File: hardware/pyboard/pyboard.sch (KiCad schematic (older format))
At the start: 71 parts, among them J1 Battery, J10 P9-P10, J2 Y1-Y8, J3 X9-X16, J4 P1-P8, J5 X17-X24, J6 USB_B_Micro, J7 Y9-Y16, J8 X1-X8, J9 Micro_SD_SCHA5B0200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

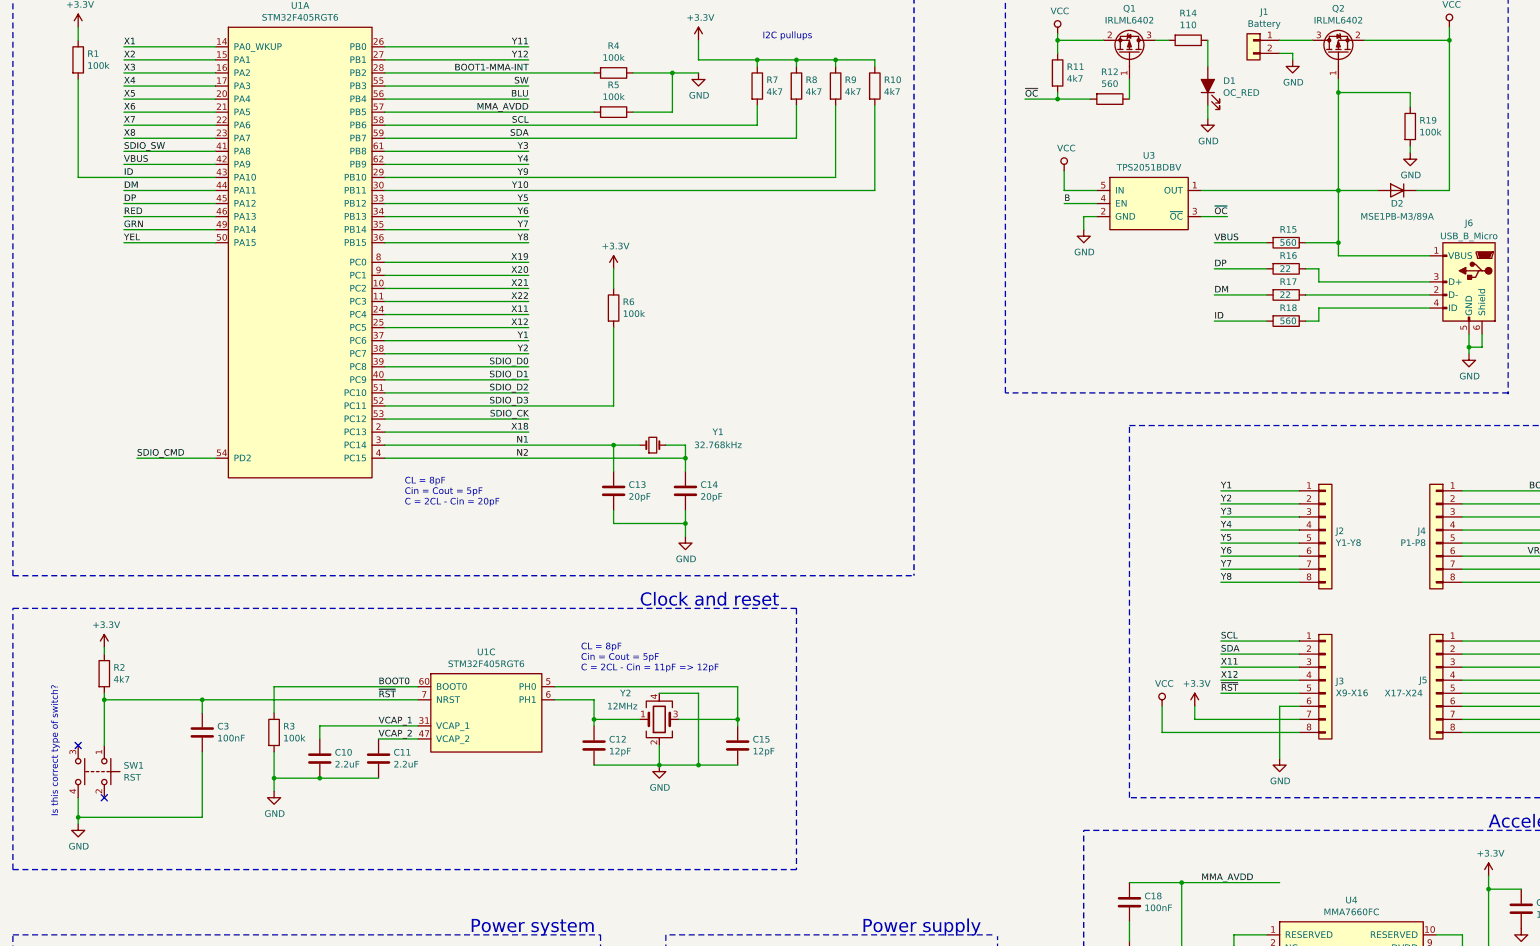
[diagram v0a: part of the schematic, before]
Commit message: Add pushbutton footprint
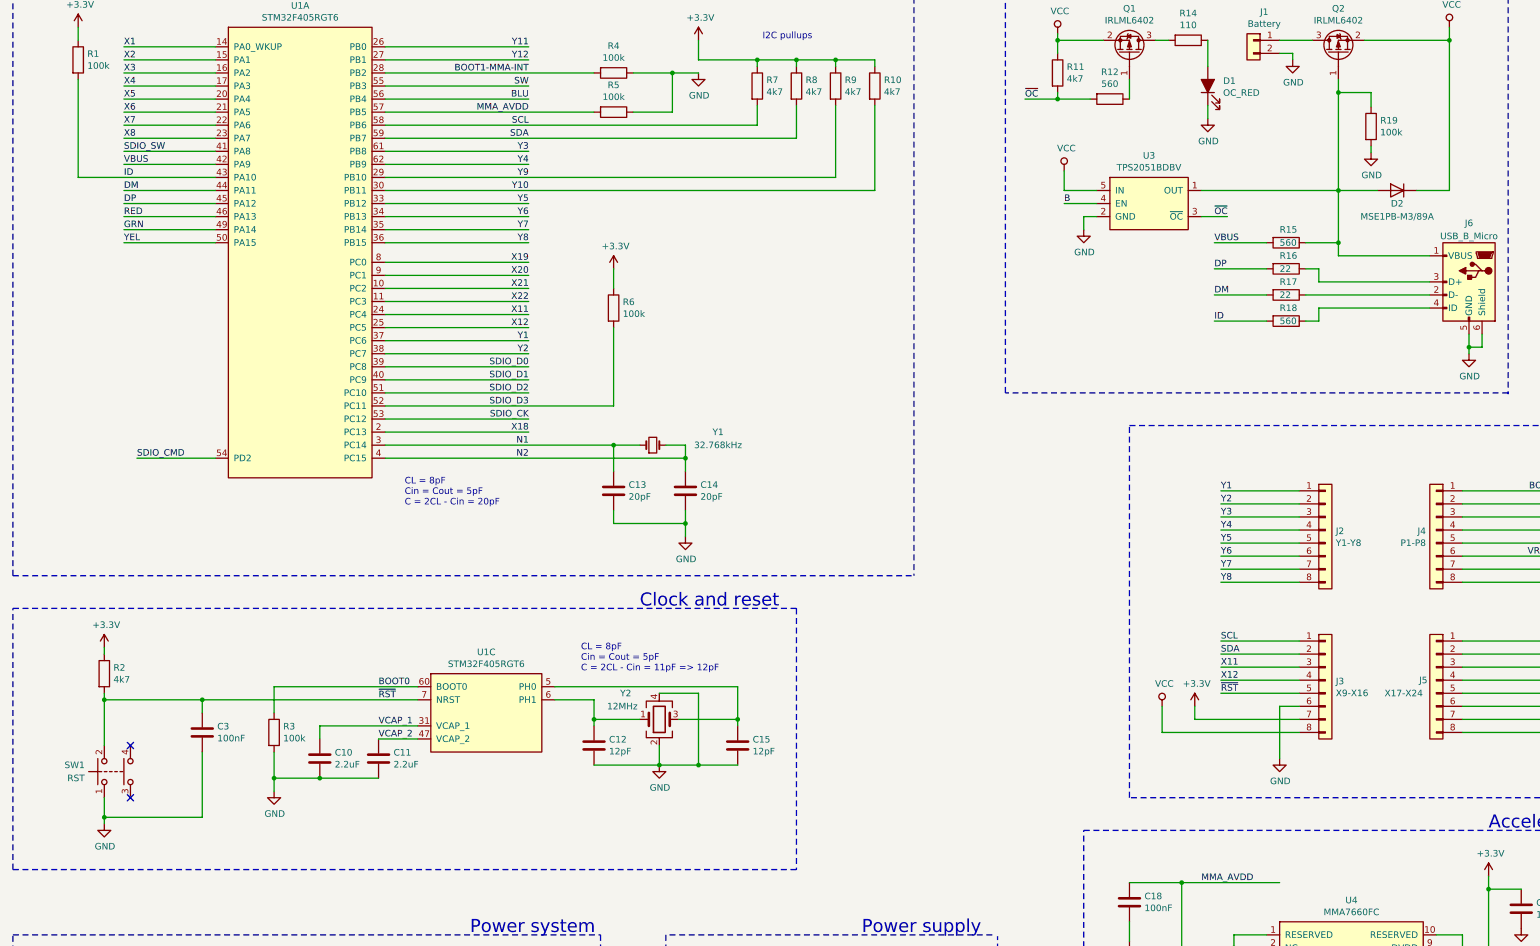
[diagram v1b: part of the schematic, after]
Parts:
- SW1, SW2: footprint (none) -> Button_Switch_SMD:SW_Push_1P1T_NO_6x6mm_H9.5mm
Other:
- note removed: "Is this correct type of switch?\n"
- moved on the sheet: R19
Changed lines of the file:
@@
 L power:GND #PWR02
 U 1 1 5D83EE79
-P 1100 7150
-F 0 "#PWR02" H 1100 6900 50  0001 C CNN
-F 1 "GND" H 1105 6977 50  0000 C CNN
-F 2 "" H 1100 7150 50  0001 C CNN
-F 3 "" H 1100 7150 50  0001 C CNN
-	1    1100 7150
-	1    0    0    -1
-$EndComp
-Wire Wire Line
-	1100 7150 1100 7100
-NoConn ~ 1300 6950
-NoConn ~ 1100 6550
+P 1300 7150
+F 0 "#PWR02" H 1300 6900 50  0001 C CNN
+F 1 "GND" H 1305 6977 50  0000 C CNN
+F 2 "" H 1300 7150 50  0001 C CNN
+F 3 "" H 1300 7150 50  0001 C CNN
+	1    1300 7150
+	1    0    0    -1
+$EndComp
+Wire Wire Line
+	1300 7150 1300 7100
 Wire Wire Line
 	1300 6200 1300 6550
@@
 	1300 6150 1300 6200
 Connection ~ 1300 6200
-Connection ~ 1100 7100
-Wire Wire Line
-	1100 7100 1100 6950
+Connection ~ 1300 7100
+Wire Wire Line
+	1300 7100 1300 6950
 Wire Wire Line
 	1300 6200 2050 6200
@@
 	2050 6600 2050 7100
 Wire Wire Line
-	1100 7100 2050 7100
+	1300 7100 2050 7100
 Wire Wire Line
 	3700 6100 2600 6100
@@
 Wire Wire Line
 	5850 1150 5850 1300
-Text Notes 950  7100 1    50   ~ 0
-Is this correct type of switch?\n
 Wire Wire Line
 	2700 8450 2700 8550
@@
 F 0 "SW2" V 9550 10550 50  0000 L CNN
 F 1 "USR" V 9450 10550 50  0000 L CNN
-F 2 "" H 9500 10600 50  0001 C CNN
+F 2 "Button_Switch_SMD:SW_Push_1P1T_NO_6x6mm_H9.5mm" H 9500 10600 50  0001 C CNN
 F 3 "~" H 9500 10600 50  0001 C CNN
 	1    9500 10400
@@
 $EndComp
 $Comp
-L Switch:SW_Push_Dual SW1
-U 1 1 5D83DA0C
-P 1300 6750
-F 0 "SW1" V 1254 6898 50  0000 L CNN
-F 1 "RST" V 1345 6898 50  0000 L CNN
-F 2 "" H 1300 6950 50  0001 C CNN
-F 3 "~" H 1300 6950 50  0001 C CNN
-	1    1300 6750
-	0    1    1    0
-$EndComp
-$Comp
 L Device:C C17
 U 1 1 5D827D89
@@
 	10750 1450 10750 1550
 Wire Wire Line
-	10750 1550 11300 1550
-Wire Wire Line
-	11300 1550 11300 1660
+	11000 1550 11000 1660
 $Comp
 L power:GND #PWR030
 U 1 1 5D98893C
-P 11300 2010
-F 0 "#PWR030" H 11300 1760 50  0001 C CNN
-F 1 "GND" H 11305 1837 50  0000 C CNN
-F 2 "" H 11300 2010 50  0001 C CNN
-F 3 "" H 11300 2010 50  0001 C CNN
-	1    11300 2010
-	1    0    0    -1
-$EndComp
-Wire Wire Line
-	11300 2010 11300 1960
+P 11000 2010
+F 0 "#PWR030" H 11000 1760 50  0001 C CNN
+F 1 "GND" H 11005 1837 50  0000 C CNN
+F 2 "" H 11000 2010 50  0001 C CNN
+F 3 "" H 11000 2010 50  0001 C CNN
+	1    11000 2010
+	1    0    0    -1
+$EndComp
+Wire Wire Line
+	11000 2010 11000 1960
 $Comp
 L Device:R R19
 U 1 1 5D983925
-P 11300 1810
-F 0 "R19" H 11370 1856 50  0000 L CNN
-F 1 "100k" H 11370 1765 50  0000 L CNN
-F 2 "Resistor_SMD:R_0603_1608Metric" V 11230 1810 50  0001 C CNN
-F 3 "~" H 11300 1810 50  0001 C CNN
-	1    11300 1810
+P 11000 1810
+F 0 "R19" H 11070 1856 50  0000 L CNN
+F 1 "100k" H 11070 1765 50  0000 L CNN
+F 2 "Resistor_SMD:R_0603_1608Metric" V 10930 1810 50  0001 C CNN
+F 3 "~" H 11000 1810 50  0001 C CNN
+	1    11000 1810
 	1    0    0    -1
 $EndComp
@@
 F 1 "TPS2051BDBV" H 9300 2676 50  0000 C CNN
 F 2 "Package_TO_SOT_SMD:SOT-23-5" H 9300 2400 50  0001 C CNN
-F 3 "" H 9300 2400 50  0001 C CNN
+F 3 "https://static.chipdip.ru/lib/120/DOC001120934.pdf" H 9300 2400 50  0001 C CNN
 	1    9300 2400
 	1    0    0    -1
@@
 Text Notes 13960 2450 0    50   ~ 0
 Which detection line should be used???\n
+Wire Wire Line
+	10750 1550 11000 1550
+NoConn ~ 1500 6550
+NoConn ~ 1500 6950
+$Comp
+L Switch:SW_Push_Dual SW1
+U 1 1 5DCFF317
+P 1300 6750
+F 0 "SW1" V 1350 6900 50  0000 L CNN
+F 1 "RST" V 1250 6900 50  0000 L CNN
+F 2 "Button_Switch_SMD:SW_Push_1P1T_NO_6x6mm_H9.5mm" H 1300 6950 50  0001 C CNN
+F 3 "~" H 1300 6950 50  0001 C CNN
+	1    1300 6750
+	0    -1   -1   0
+$EndComp
 $EndSCHEMATC

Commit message: Add footprint for battery cell
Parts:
- removed J10: P9-P10, symbol Connector_Generic:Conn_02x04_Counter_Clockwise
- removed J2: Y1-Y8, symbol Connector_Generic:Conn_01x08
- removed J3: X9-X16, symbol Connector_Generic:Conn_01x08
- removed J4: P1-P8, symbol Connector_Generic:Conn_01x08
- removed J5: X17-X24, symbol Connector_Generic:Conn_01x08
- removed J7: Y9-Y16, symbol Connector_Generic:Conn_01x08
- removed J8: X1-X8, symbol Connector_Generic:Conn_01x08
- added J2: Arduino_Mega2560_Shield, components:Arduino_Mega2560_Shield, symbol components:Arduino_Mega2560_Shield
- J1: footprint (none) -> components:CH224-2032LF
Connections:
- wire segments 349 -> 377
- no-connect marks 4 -> 46
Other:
- note added: "Shield\n"
- note removed: "Connectors"
- moved on the sheet: C1, C10, C11, C12, C13, C14, C15, C16, C17, C18, C19, C2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

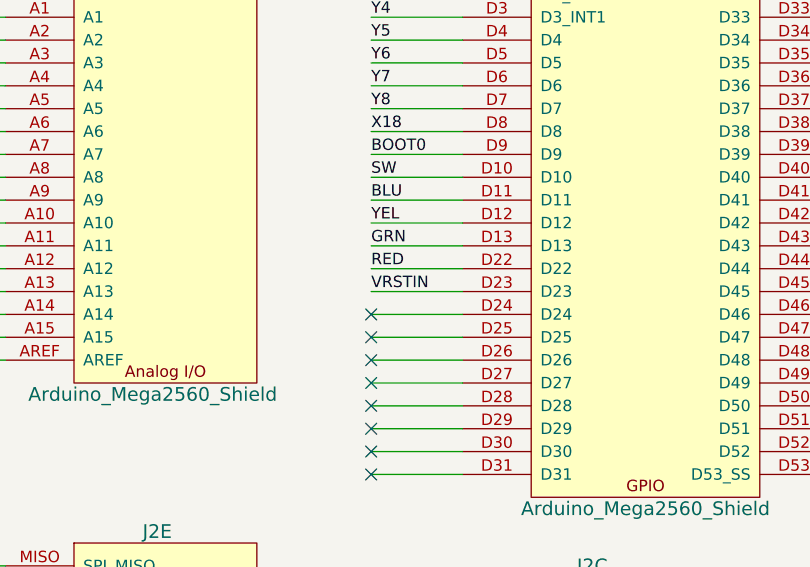
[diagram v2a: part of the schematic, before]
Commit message: Fix dangling pin
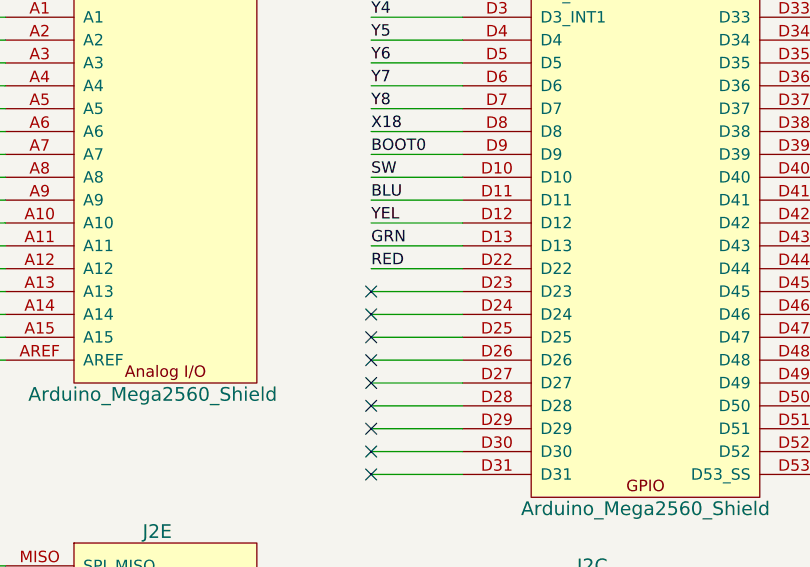
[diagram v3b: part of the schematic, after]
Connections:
- net VRSTIN: no longer names the net of J2.D23
- no-connect marks 46 -> 47
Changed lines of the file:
@@
 Text Label 19450 5550 0    50   ~ 0
 RED
-Text Label 19450 5650 0    50   ~ 0
-VRSTIN
 Wire Wire Line
 	19850 5150 19450 5150
@@
 Text Notes 21550 4000 0    100  ~ 0
 Shield\n
+NoConn ~ 19450 5650
 $EndSCHEMATC

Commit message: Generate netlist and place fixed components
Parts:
- SW1, SW2: symbol Switch:SW_Push_Dual -> Switch:SW_Push
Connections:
- net labels added: DM_USB, DP_USB, ID_USB, VBUS_USB
- no-connect marks 47 -> 43
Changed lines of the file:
@@
 Wire Wire Line
 	4700 14350 4700 14550
-NoConn ~ 4900 14350
-NoConn ~ 4900 13950
 Wire Wire Line
 	4700 13550 4700 13950
@@
 $EndComp
 $Comp
-L Switch:SW_Push_Dual SW2
+L Switch:SW_Push SW2
 U 1 1 5D8FF238
 P 4700 14150
@@
 Wire Wire Line
 	11550 1800 11800 1800
-NoConn ~ 1900 7550
-NoConn ~ 1900 7950
-$Comp
-L Switch:SW_Push_Dual SW1
+$Comp
+L Switch:SW_Push SW1
 U 1 1 5DCFF317
 P 1700 7750
@@
 Shield\n
 NoConn ~ 19450 5650
+Text Label 11850 3050 0    50   ~ 0
+VBUS_USB
+Text Label 11850 3250 0    50   ~ 0
+DP_USB
+Text Label 11850 3350 0    50   ~ 0
+DM_USB
+Text Label 11850 3450 0    50   ~ 0
+ID_USB
 $EndSCHEMATC
